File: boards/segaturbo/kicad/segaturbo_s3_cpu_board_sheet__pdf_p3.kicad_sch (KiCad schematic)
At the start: 34 parts, among them CN9 Conn_02x30, IC10 AM2919, IC11 74LS283, IC12 93419, IC22 PAL16R4, IC23 AM2919, IC24 74LS283, IC25 74LS258, IC26 74LS258, IC35a 74LS74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

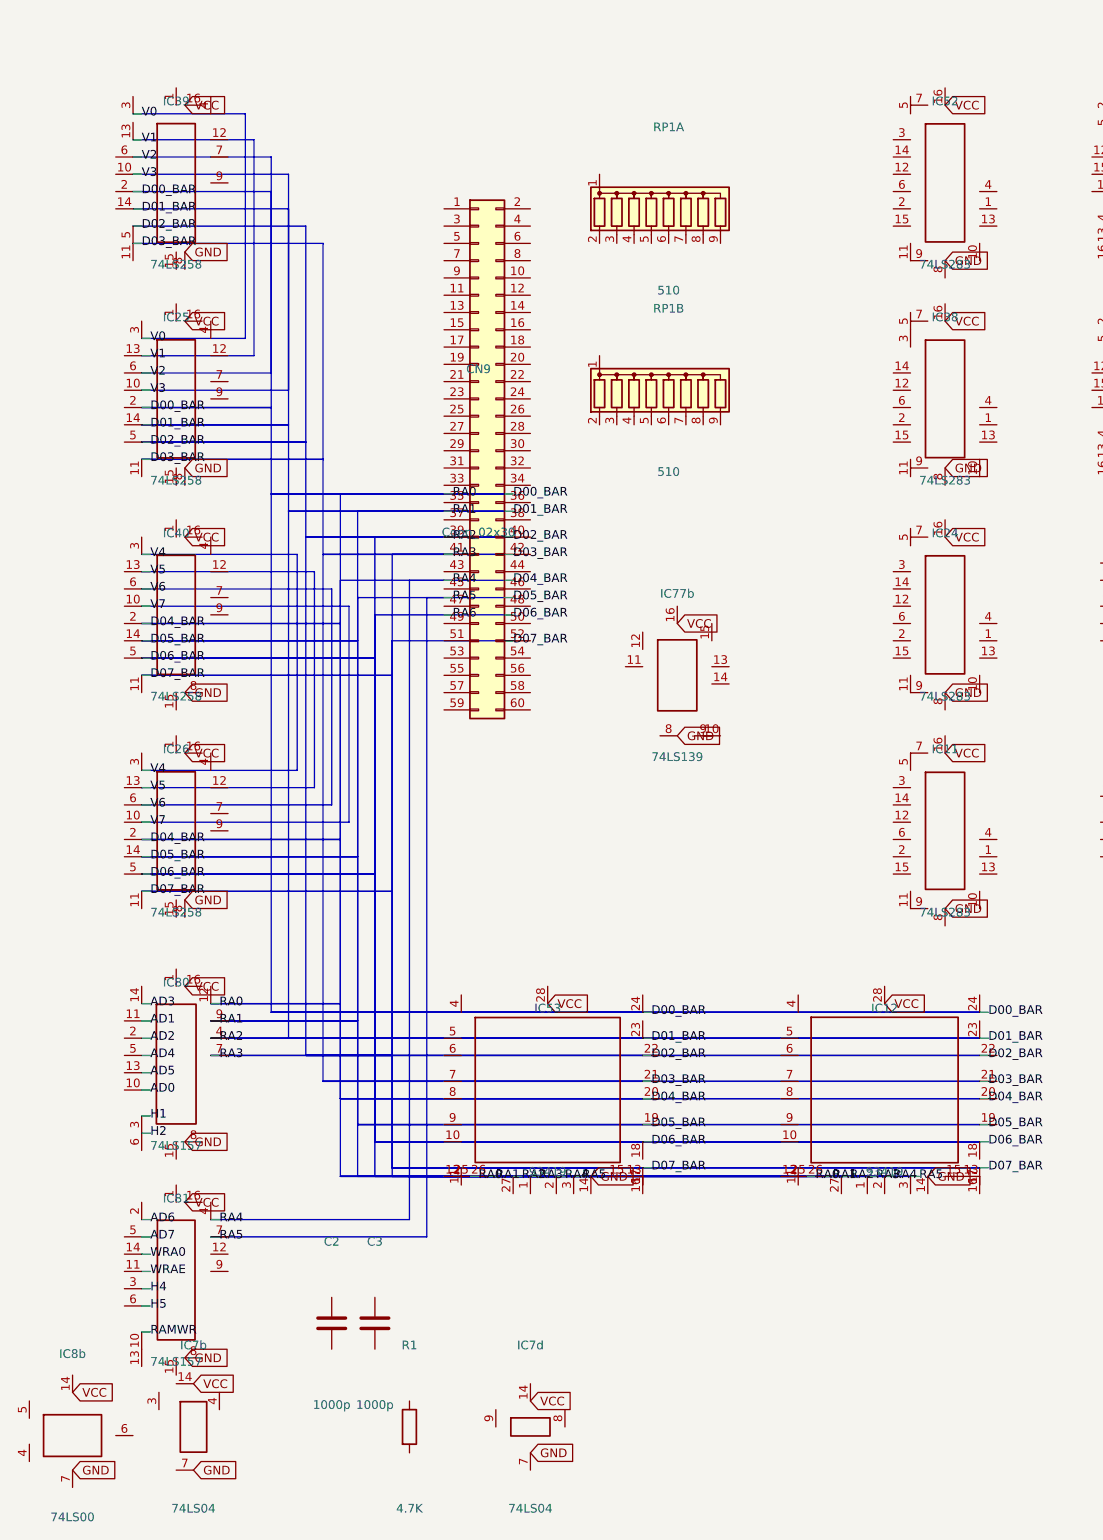
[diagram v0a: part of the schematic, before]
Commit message: Fix KiCad pin-aligned generated symbols
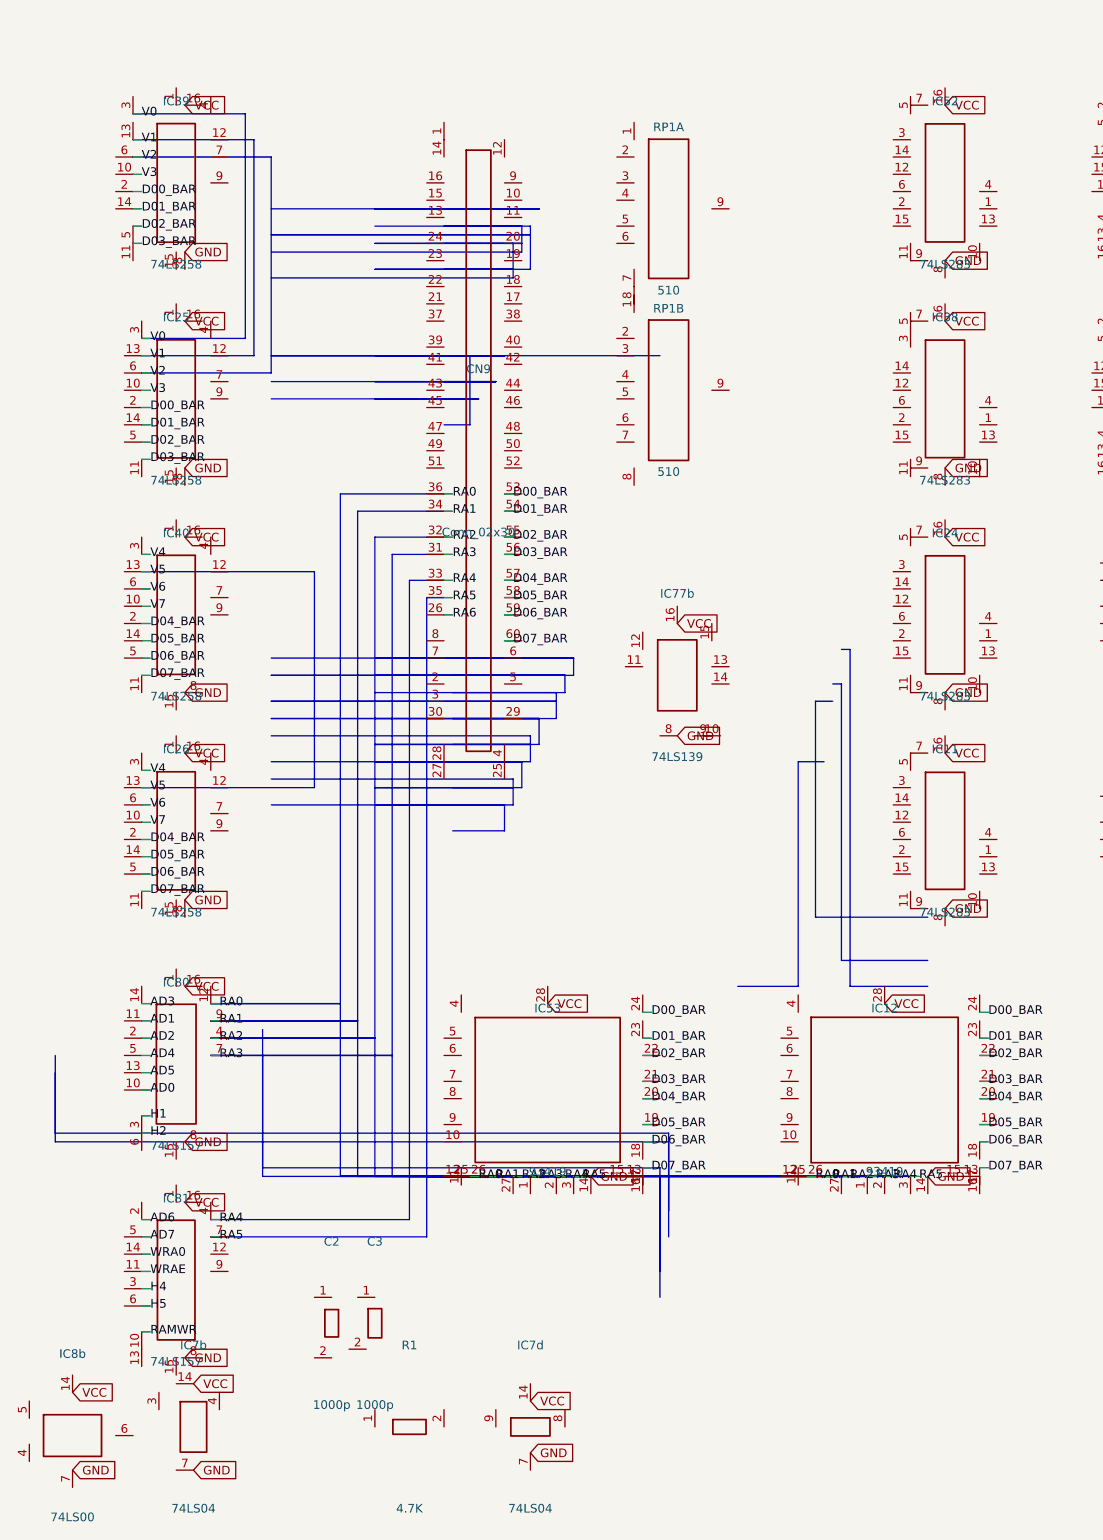
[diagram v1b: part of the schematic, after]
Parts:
- C2: symbol Device:C -> user:_chip_C2
- C3: symbol Device:C -> user:_chip_C3
- CN9: symbol Connector_Generic:Conn_02x30_Odd_Even -> user:_chip_CN9
- R1: symbol Device:R -> user:_chip_R1
- RP1A: symbol Device:R_Network08 -> user:_chip_RP1A
- RP1B: symbol Device:R_Network08 -> user:_chip_RP1B
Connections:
- net D00_BAR: now also CN9.53
- net D01_BAR: now also CN9.54
- net D02_BAR: now also CN9.55
- net D03_BAR: now also CN9.56
- net D04_BAR: now also CN9.57
- net D05_BAR: now also CN9.58
- net D06_BAR: now also CN9.59
- net D07_BAR: now also CN9.60
- net RA0: now also CN9.36
- net RA1: now also CN9.34
- net RA2: now also CN9.32; no longer CN9.39 (Pin_39)
- net RA3: now also CN9.31; no longer CN9.41 (Pin_41)
- net RA4: now also CN9.33
- net RA5: now also CN9.35
- net RA6: now also CN9.26
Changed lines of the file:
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@@
   )
   (symbol
-    (lib_id "Device:R")
+    (lib_id "user:_chip_R1")
     (at 119.38 240.03 0)
     (unit 1)
@@
   )
   (symbol
-    (lib_id "Device:C")
+    (lib_id "user:_chip_C2")
     (at 107.95 224.79 0)
     (unit 1)
@@
   )
   (symbol
-    (lib_id "Device:C")
+    (lib_id "user:_chip_C3")
     (at 114.3 224.79 0)
     (unit 1)
@@
   )
   (symbol
-    (lib_id "Connector_Generic:Conn_02x30_Odd_Even")
+    (lib_id "user:_chip_CN9")
     (at 129.54 96.52 0)
     (unit 1)
@@
   )
   (symbol
-    (lib_id "Device:R_Network08")
+    (lib_id "user:_chip_RP1A")
     (at 157.48 60.96 0)
     (unit 1)
@@
   )
   (symbol
-    (lib_id "Device:R_Network08")
+    (lib_id "user:_chip_RP1B")
     (at 157.48 87.63 0)
     (unit 1)
@@
     (stroke (width 0) (type default))
   )
-  (polyline (pts (xy 78.74 58.42) (xy 99.06 58.42) (xy 99.06 90.17) (xy 80.01 90.17) (xy 99.06 90.17) (xy 99.06 102.87) (xy 133.35 102.87) (xy 99.06 102.87) (xy 99.06 179.07) (xy 203.2 179.07) (xy 99.06 179.07) (xy 99.06 179.07) (xy 153.67 179.07))
-    (stroke (width 0.1524) (type default))
-    (fill (type none))
-  )
-  (polyline (pts (xy 78.74 60.96) (xy 101.6 60.96) (xy 101.6 92.71) (xy 80.01 92.71) (xy 101.6 92.71) (xy 101.6 105.41) (xy 133.35 105.41) (xy 101.6 105.41) (xy 101.6 182.88) (xy 203.2 182.88) (xy 101.6 182.88) (xy 101.6 182.88) (xy 153.67 182.88))
-    (stroke (width 0.1524) (type default))
-    (fill (type none))
-  )
-  (polyline (pts (xy 78.74 63.5) (xy 104.14 63.5) (xy 104.14 95.25) (xy 80.01 95.25) (xy 104.14 95.25) (xy 104.14 109.22) (xy 133.35 109.22) (xy 104.14 109.22) (xy 104.14 185.42) (xy 203.2 185.42) (xy 104.14 185.42) (xy 104.14 185.42) (xy 153.67 185.42))
-    (stroke (width 0.1524) (type default))
-    (fill (type none))
-  )
-  (polyline (pts (xy 78.74 66.04) (xy 106.68 66.04) (xy 106.68 97.79) (xy 80.01 97.79) (xy 106.68 97.79) (xy 106.68 111.76) (xy 133.35 111.76) (xy 106.68 111.76) (xy 106.68 189.23) (xy 203.2 189.23) (xy 106.68 189.23) (xy 106.68 189.23) (xy 153.67 189.23))
-    (stroke (width 0.1524) (type default))
-    (fill (type none))
-  )
-  (polyline (pts (xy 133.35 115.57) (xy 109.22 115.57) (xy 109.22 121.92) (xy 80.01 121.92) (xy 109.22 121.92) (xy 109.22 153.67) (xy 80.01 153.67) (xy 109.22 153.67) (xy 109.22 191.77) (xy 203.2 191.77) (xy 109.22 191.77) (xy 109.22 191.77) (xy 153.67 191.77))
-    (stroke (width 0.1524) (type default))
-    (fill (type none))
-  )
-  (polyline (pts (xy 133.35 118.11) (xy 111.76 118.11) (xy 111.76 124.46) (xy 80.01 124.46) (xy 111.76 124.46) (xy 111.76 156.21) (xy 80.01 156.21) (xy 111.76 156.21) (xy 111.76 195.58) (xy 203.2 195.58) (xy 111.76 195.58) (xy 111.76 195.58) (xy 153.67 195.58))
-    (stroke (width 0.1524) (type default))
-    (fill (type none))
-  )
-  (polyline (pts (xy 133.35 120.65) (xy 114.3 120.65) (xy 114.3 127) (xy 80.01 127) (xy 114.3 127) (xy 114.3 158.75) (xy 80.01 158.75) (xy 114.3 158.75) (xy 114.3 198.12) (xy 203.2 198.12) (xy 114.3 198.12) (xy 114.3 198.12) (xy 153.67 198.12))
-    (stroke (width 0.1524) (type default))
-    (fill (type none))
-  )
-  (polyline (pts (xy 133.35 124.46) (xy 116.84 124.46) (xy 116.84 129.54) (xy 80.01 129.54) (xy 116.84 129.54) (xy 116.84 161.29) (xy 80.01 161.29) (xy 116.84 161.29) (xy 116.84 201.93) (xy 203.2 201.93) (xy 116.84 201.93) (xy 116.84 201.93) (xy 153.67 201.93))
-    (stroke (width 0.1524) (type default))
-    (fill (type none))
-  )
-  (polyline (pts (xy 78.74 55.88) (xy 101.6 55.88) (xy 101.6 87.63) (xy 80.01 87.63))
-    (stroke (width 0.1524) (type default))
-    (fill (type none))
-  )
-  (polyline (pts (xy 80.01 111.76) (xy 102.87 111.76) (xy 102.87 143.51) (xy 80.01 143.51))
+  (polyline (pts (xy 156.21 82.55) (xy 128.27 82.55) (xy 128.27 92.71) (xy 124.46 92.71))
+    (stroke (width 0.1524) (type default))
+    (fill (type none))
+  )
+  (polyline (pts (xy 114.3 88.9) (xy 129.54 88.9) (xy 129.54 88.9) (xy 124.46 88.9) (xy 129.54 88.9) (xy 129.54 88.9) (xy 99.06 88.9))
+    (stroke (width 0.1524) (type default))
+    (fill (type none))
+  )
+  (polyline (pts (xy 124.46 86.36) (xy 132.08 86.36) (xy 132.08 86.36) (xy 114.3 86.36) (xy 132.08 86.36) (xy 132.08 86.36) (xy 99.06 86.36))
+    (stroke (width 0.1524) (type default))
+    (fill (type none))
+  )
+  (polyline (pts (xy 124.46 82.55) (xy 133.35 82.55) (xy 133.35 82.55) (xy 99.06 82.55) (xy 133.35 82.55) (xy 133.35 82.55) (xy 114.3 82.55))
+    (stroke (width 0.1524) (type default))
+    (fill (type none))
+  )
+  (polyline (pts (xy 124.46 66.04) (xy 134.62 66.04) (xy 134.62 69.85) (xy 114.3 69.85) (xy 134.62 69.85) (xy 134.62 71.12) (xy 99.06 71.12))
+    (stroke (width 0.1524) (type default))
+    (fill (type none))
+  )
+  (polyline (pts (xy 124.46 63.5) (xy 135.89 63.5) (xy 135.89 66.04) (xy 114.3 66.04) (xy 135.89 66.04) (xy 135.89 67.31) (xy 99.06 67.31))
+    (stroke (width 0.1524) (type default))
+    (fill (type none))
+  )
+  (polyline (pts (xy 114.3 63.5) (xy 137.16 63.5) (xy 137.16 64.77) (xy 99.06 64.77) (xy 137.16 64.77) (xy 137.16 69.85) (xy 124.46 69.85))
+    (stroke (width 0.1524) (type default))
+    (fill (type none))
+  )
+  (polyline (pts (xy 99.06 60.96) (xy 138.43 60.96) (xy 138.43 60.96) (xy 114.3 60.96) (xy 138.43 60.96) (xy 124.46 60.96))
+    (stroke (width 0.1524) (type default))
+    (fill (type none))
+  )
+  (polyline (pts (xy 99.06 148.59) (xy 133.35 148.59) (xy 133.35 148.59) (xy 114.3 148.59) (xy 133.35 148.59) (xy 133.35 152.4) (xy 125.73 152.4))
+    (stroke (width 0.1524) (type default))
+    (fill (type none))
+  )
+  (polyline (pts (xy 99.06 144.78) (xy 134.62 144.78) (xy 134.62 146.05) (xy 114.3 146.05) (xy 134.62 146.05) (xy 134.62 148.59) (xy 125.73 148.59))
+    (stroke (width 0.1524) (type default))
+    (fill (type none))
+  )
+  (polyline (pts (xy 99.06 142.24) (xy 135.89 142.24) (xy 135.89 142.24) (xy 114.3 142.24) (xy 135.89 142.24) (xy 135.89 146.05) (xy 125.73 146.05))
+    (stroke (width 0.1524) (type default))
+    (fill (type none))
+  )
+  (polyline (pts (xy 99.06 138.43) (xy 137.16 138.43) (xy 137.16 139.7) (xy 114.3 139.7) (xy 137.16 139.7) (xy 137.16 142.24) (xy 125.73 142.24))
+    (stroke (width 0.1524) (type default))
+    (fill (type none))
+  )
+  (polyline (pts (xy 114.3 135.89) (xy 138.43 135.89) (xy 138.43 135.89) (xy 99.06 135.89) (xy 138.43 135.89) (xy 138.43 139.7) (xy 125.73 139.7))
+    (stroke (width 0.1524) (type default))
+    (fill (type none))
+  )
+  (polyline (pts (xy 114.3 132.08) (xy 140.97 132.08) (xy 140.97 133.35) (xy 99.06 133.35) (xy 140.97 133.35) (xy 140.97 135.89) (xy 125.73 135.89))
+    (stroke (width 0.1524) (type default))
+    (fill (type none))
+  )
+  (polyline (pts (xy 114.3 129.54) (xy 142.24 129.54) (xy 142.24 129.54) (xy 99.06 129.54) (xy 142.24 129.54) (xy 142.24 132.08) (xy 125.73 132.08))
+    (stroke (width 0.1524) (type default))
+    (fill (type none))
+  )
+  (polyline (pts (xy 99.06 127) (xy 143.51 127) (xy 143.51 127) (xy 114.3 127) (xy 143.51 127) (xy 143.51 129.54) (xy 125.73 129.54))
+    (stroke (width 0.1524) (type default))
+    (fill (type none))
+  )
+  (polyline (pts (xy 97.79 181.61) (xy 97.79 201.93) (xy 156.21 201.93) (xy 156.21 217.17))
+    (stroke (width 0.1524) (type default))
+    (fill (type none))
+  )
+  (polyline (pts (xy 97.79 185.42) (xy 97.79 203.2) (xy 156.21 203.2) (xy 156.21 220.98))
+    (stroke (width 0.1524) (type default))
+    (fill (type none))
+  )
+  (polyline (pts (xy 180.34 142.24) (xy 176.53 142.24) (xy 176.53 175.26) (xy 167.64 175.26))
+    (stroke (width 0.1524) (type default))
+    (fill (type none))
+  )
+  (polyline (pts (xy 181.61 133.35) (xy 179.07 133.35) (xy 179.07 165.1) (xy 195.58 165.1))
     (stroke (width 0.1524) (type default))
     (fill (type none))
@@
     (fill (type none))
   )
-  (polyline (pts (xy 80.01 116.84) (xy 107.95 116.84) (xy 107.95 148.59) (xy 80.01 148.59))
-    (stroke (width 0.1524) (type default))
-    (fill (type none))
-  )
-  (polyline (pts (xy 80.01 119.38) (xy 110.49 119.38) (xy 110.49 151.13) (xy 80.01 151.13))
+  (polyline (pts (xy 181.61 130.81) (xy 182.88 130.81) (xy 182.88 171.45) (xy 195.58 171.45))
+    (stroke (width 0.1524) (type default))
+    (fill (type none))
+  )
+  (polyline (pts (xy 182.88 125.73) (xy 184.15 125.73) (xy 184.15 175.26) (xy 195.58 175.26))
     (stroke (width 0.1524) (type default))
     (fill (type none))
@@
     (fill (type none))
   )
+  (polyline (pts (xy 67.31 187.96) (xy 67.31 198.12) (xy 157.48 198.12) (xy 157.48 212.09))
+    (stroke (width 0.1524) (type default))
+    (fill (type none))
+  )
   (polyline (pts (xy 233.68 46.99) (xy 247.65 46.99) (xy 247.65 132.08) (xy 279.4 132.08))
     (stroke (width 0.1524) (type default))
@@
     (stroke (width 0.1524) (type default))
     (fill (type none))
+  )
+  (polyline (pts (xy 67.31 185.42) (xy 67.31 196.85) (xy 157.48 196.85) (xy 157.48 208.28))
+    (stroke (width 0.1524) (type default))
+    (fill (type none))
